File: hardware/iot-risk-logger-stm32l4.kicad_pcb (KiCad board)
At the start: 2 copper layers, 55 x 45 mm, 52 parts, among them J1 USB Type-C, J2 TagConnect SWD ARM, Q1 IRLML6401, U1 ST25DV04K, U2 OPT3001DNPR, U3 SHT30-DIS, U4 LIS2DW12, U5 AP2112K-3.3, U6 W25Q64JV, U7 STM32L412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

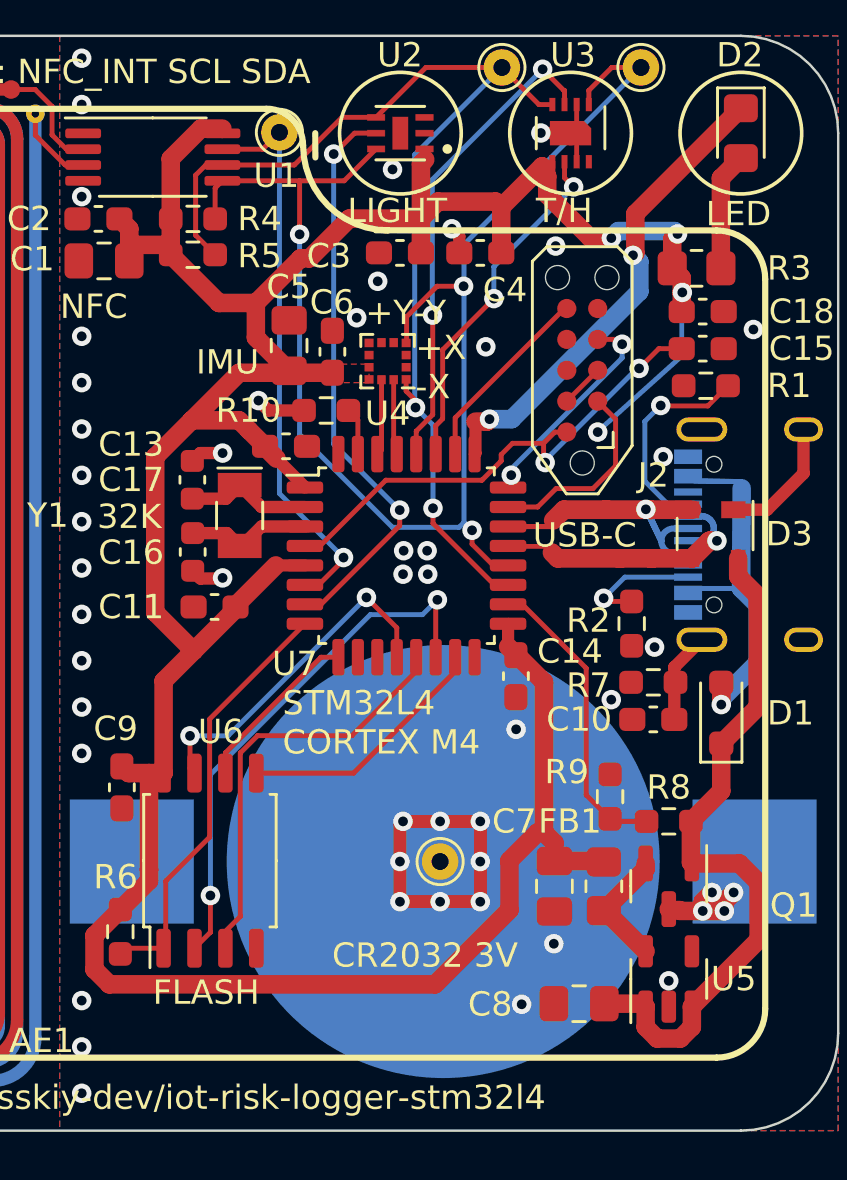
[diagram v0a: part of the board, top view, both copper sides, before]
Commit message: README: add dev tools table
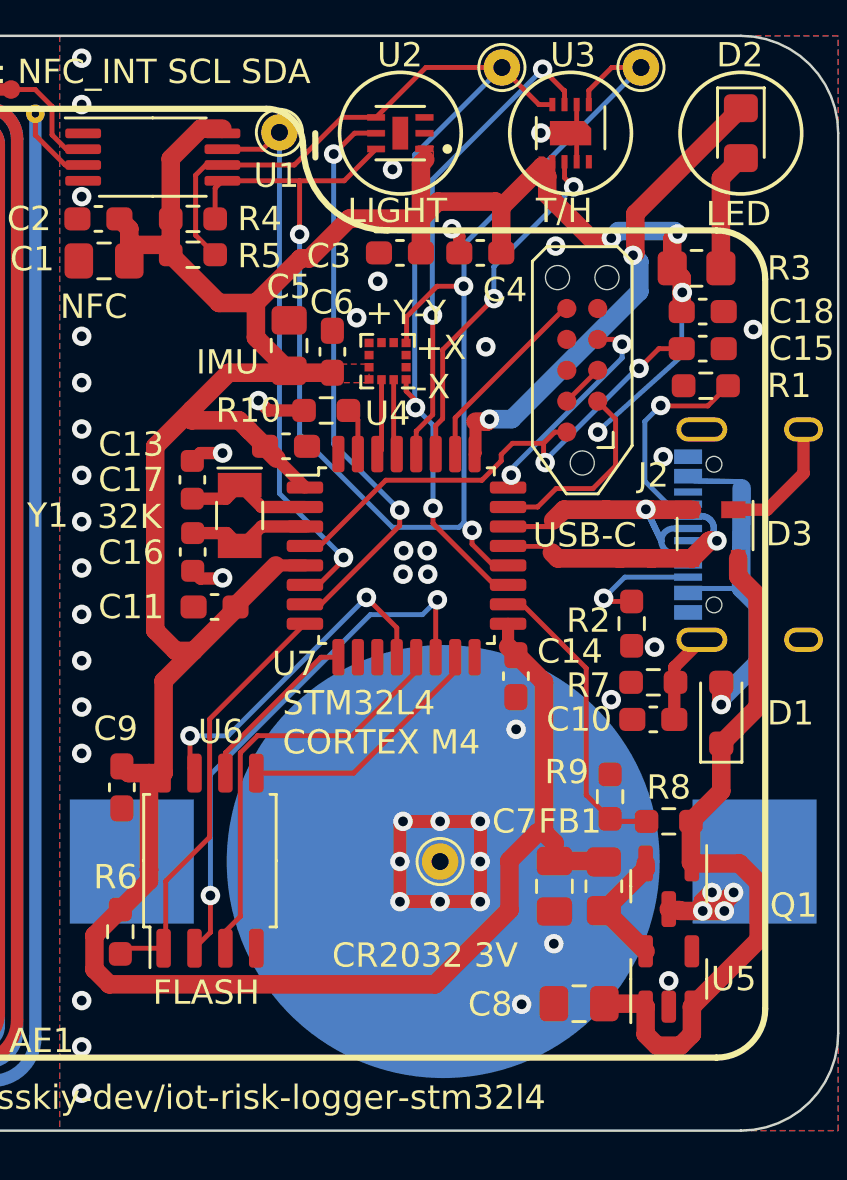
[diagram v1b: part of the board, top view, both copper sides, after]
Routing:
- net VDD: track 139.4 -> 140.5 mm
- net +5V: track 29.0 -> 29.6 mm
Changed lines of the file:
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@@
         (effects (font (size 1 1) (thickness 0.15)))
     )
-    (fp_text value "Antenna_Loop" (at -20 -20.25 unlocked) (layer "F.Fab")
+    (fp_text value "Antenna_Loop" (at -20 -20.25 unlocked) (layer "F.Fab") hide
         (effects (font (size 1 1) (thickness 0.15)))
     )
-    (fp_text user "20mil line + 10 mil spacing" (at -11.25 -25 unlocked) (layer "Dwgs.User")
+    (fp_text user "20mil line + 10 mil spacing" (at -11.25 -25 unlocked) (layer "Dwgs.User") hide
         (effects (font (size 1 1) (thickness 0.15)) (justify left bottom))
     )
-    (fp_text user "1 layer ~ 1.4uH, double layer 1.4*~3.5=~4.9uH" (at -18.25 -27 unlocked) (layer "Dwgs.User")
+    (fp_text user "1 layer ~ 1.4uH, double layer 1.4*~3.5=~4.9uH" (at -18.25 -27 unlocked) (layer "Dwgs.User") hide
         (effects (font (size 1 1) (thickness 0.15)) (justify left bottom))
     )
-    (fp_text user "${REFERENCE}" (at -24 -18.25 unlocked) (layer "F.Fab")
+    (fp_text user "${REFERENCE}" (at -24 -18.25 unlocked) (layer "F.Fab") hide
         (effects (font (size 1 1) (thickness 0.15)))
     )
@@
   (segment (start 130.8608 66.0913) (end 132.5645 66.0913) (width 0.762) (layer "F.Cu") (net 10))
   (segment (start 130.8305 87.804) (end 130.556 87.5295) (width 0.762) (layer "F.Cu") (net 10))
+  (segment (start 131.9276 74.3712) (end 133.423942 72.874858) (width 0.762) (layer "F.Cu") (net 10))
   (segment (start 146.7518 82.9323) (end 146.431 82.6115) (width 0.762) (layer "F.Cu") (net 10))
   (segment (start 132.5645 62.5494) (end 132.5645 65.024) (width 0.762) (layer "F.Cu") (net 10))
@@
   (segment (start 146.4872 91.4015) (end 146.4872 93.4308) (width 0.762) (layer "F.Cu") (net 10))
   (segment (start 138.081 76.0447) (end 138.081 76.067) (width 0.5008) (layer "F.Cu") (net 10))
+  (segment (start 133.423942 73.3044) (end 133.423942 72.874858) (width 0.762) (layer "F.Cu") (net 10))
   (segment (start 130.8608 65.4315) (end 130.8608 66.0913) (width 0.762) (layer "F.Cu") (net 10))
   (segment (start 142.8485 66.276) (end 142.8485 66.421) (width 0.762) (layer "F.Cu") (net 10))
@@
   (segment (start 142.848 66.2755) (end 142.8485 66.276) (width 0.762) (layer "F.Cu") (net 10))
   (segment (start 146.1505 65.717) (end 146.1505 66.421) (width 0.762) (layer "F.Cu") (net 10))
-  (segment (start 133.423942 73.3044) (end 135.380842 71.3475) (width 0.762) (layer "F.Cu") (net 10))
   (segment (start 132.271 84.0187) (end 133.5074 82.7823) (width 0.762) (layer "F.Cu") (net 10))
   (segment (start 134.6885 61.3125) (end 133.8014 61.3125) (width 0.762) (layer "F.Cu") (net 10))
@@
   (segment (start 142.995 62.6176) (end 142.995 62.15) (width 0.2698) (layer "F.Cu") (net 10))
   (segment (start 131.6716 91.7681) (end 131.6701 91.7696) (width 0.762) (layer "F.Cu") (net 10))
-  (segment (start 135.380842 71.3475) (end 137.43 71.3475) (width 0.762) (layer "F.Cu") (net 10))
   (segment (start 145.9208 64.3128) (end 143.5473 64.3128) (width 0.762) (layer "F.Cu") (net 10))
   (segment (start 136.9177 74.8814) (end 138.081 76.0447) (width 0.5008) (layer "F.Cu") (net 10))
@@
   (segment (start 135.2285 80.9218) (end 136.8833 79.267) (width 0.762) (layer "F.Cu") (net 10))
   (segment (start 150.3305 91.4185) (end 150.368 91.456) (width 0.762) (layer "F.Cu") (net 10))
+  (segment (start 131.9276 81.9404) (end 131.9276 74.3712) (width 0.762) (layer "F.Cu") (net 10))
   (segment (start 137.8989 66.646) (end 138.27 66.646) (width 0.762) (layer "F.Cu") (net 10))
   (segment (start 146.4872 93.4308) (end 143.4312 96.4868) (width 0.762) (layer "F.Cu") (net 10))
   (segment (start 135.2285 80.9752) (end 135.2285 80.9218) (width 0.762) (layer "F.Cu") (net 10))
   (segment (start 153.178 65.8619) (end 153.178 67.056) (width 0.762) (layer "F.Cu") (net 10))
+  (segment (start 132.7695 82.7823) (end 131.9276 81.9404) (width 0.762) (layer "F.Cu") (net 10))
   (segment (start 153.5695 68.0223) (end 153.5695 67.4475) (width 0.762) (layer "F.Cu") (net 10))
   (segment (start 136.8833 79.267) (end 138.081 79.267) (width 0.5008) (layer "F.Cu") (net 10))
@@
   (segment (start 148.336 91.4185) (end 150.3305 91.4185) (width 0.762) (layer "F.Cu") (net 10))
   (segment (start 138.27 66.646) (end 139.9039 65.0121) (width 0.762) (layer "F.Cu") (net 10))
-  (segment (start 131.9276 74.800742) (end 133.423942 73.3044) (width 0.762) (layer "F.Cu") (net 10))
   (segment (start 130.0402 96.4868) (end 129.4288 95.8754) (width 0.762) (layer "F.Cu") (net 10))
   (segment (start 130.8608 66.0913) (end 130.8608 66.7512) (width 0.762) (layer "F.Cu") (net 10))
@@
   (segment (start 147.6498 90.2389) (end 146.4872 91.4015) (width 0.762) (layer "F.Cu") (net 10))
   (segment (start 153.5695 67.4475) (end 153.178 67.056) (width 0.762) (layer "F.Cu") (net 10))
+  (segment (start 133.423942 72.874858) (end 134.9513 71.3475) (width 0.762) (layer "F.Cu") (net 10))
   (segment (start 131.6716 87.804) (end 131.6716 91.7681) (width 0.762) (layer "F.Cu") (net 10))
   (segment (start 148.25 62.675) (end 148.25 63.28) (width 0.2498) (layer "F.Cu") (net 10))
   (segment (start 136.9177 74.8814) (end 136.4405 74.4042) (width 0.762) (layer "F.Cu") (net 10))
+  (segment (start 133.5074 82.7823) (end 132.7695 82.7823) (width 0.762) (layer "F.Cu") (net 10))
   (segment (start 136.0644 69.9029) (end 137.43 71.2685) (width 0.762) (layer "F.Cu") (net 10))
   (segment (start 139.9039 65.0121) (end 142.848 65.0121) (width 0.762) (layer "F.Cu") (net 10))
   (segment (start 146.8022 82.9575) (end 146.7518 82.9575) (width 0.762) (layer "F.Cu") (net 10))
+  (segment (start 134.9513 71.3475) (end 137.43 71.3475) (width 0.762) (layer "F.Cu") (net 10))
   (segment (start 129.4288 94.4767) (end 130.493 93.4125) (width 0.762) (layer "F.Cu") (net 10))
   (segment (start 129.4288 95.8754) (end 129.4288 94.4767) (width 0.762) (layer "F.Cu") (net 10))
@@
   (segment (start 153.3959 65.644) (end 153.178 65.8619) (width 0.762) (layer "F.Cu") (net 10))
   (segment (start 143.4312 96.4868) (end 130.0402 96.4868) (width 0.762) (layer "F.Cu") (net 10))
-  (segment (start 133.5074 82.7823) (end 131.9276 81.2025) (width 0.762) (layer "F.Cu") (net 10))
   (segment (start 135.3737 73.3044) (end 135.7829 73.7136) (width 0.762) (layer "F.Cu") (net 10))
   (segment (start 153.5695 68.0709) (end 153.5938 68.0466) (width 0.762) (layer "F.Cu") (net 10))
-  (segment (start 131.9276 81.2025) (end 131.9276 74.800742) (width 0.762) (layer "F.Cu") (net 10))
   (segment (start 149.8182 65.8123) (end 148.0404 64.0345) (width 0.762) (layer "F.Cu") (net 10))
   (segment (start 136.0644 68.4805) (end 136.0644 69.9029) (width 0.762) (layer "F.Cu") (net 10))
@@
   (segment (start 155.89 78.978) (end 155.89 79.7154) (width 0.762) (layer "F.Cu") (net 31))
   (segment (start 155.9411 91.5185) (end 153.985 91.5185) (width 0.762) (layer "F.Cu") (net 31))
-  (segment (start 153.985 98.2431) (end 153.985 97.4035) (width 0.762) (layer "F.Cu") (net 31))
+  (segment (start 153.985 98.5418) (end 153.985 97.4035) (width 0.762) (layer "F.Cu") (net 31))
   (segment (start 153.985 91.5185) (end 153.9475 91.481) (width 0.762) (layer "F.Cu") (net 31))
-  (segment (start 152.085 97.4035) (end 152.085 98.2422) (width 0.762) (layer "F.Cu") (net 31))
-  (segment (start 152.5581 98.7153) (end 153.5128 98.7153) (width 0.762) (layer "F.Cu") (net 31))
   (segment (start 151.9635 97.282) (end 152.085 97.4035) (width 0.762) (layer "F.Cu") (net 31))
   (segment (start 153.9475 91.481) (end 153.9475 89.789) (width 0.762) (layer "F.Cu") (net 31))
+  (segment (start 152.085 98.5418) (end 152.5524 99.0092) (width 0.762) (layer "F.Cu") (net 31))
+  (segment (start 152.5524 99.0092) (end 153.5176 99.0092) (width 0.762) (layer "F.Cu") (net 31))
+  (segment (start 152.085 97.4035) (end 152.085 98.5418) (width 0.762) (layer "F.Cu") (net 31))
   (segment (start 155.194 86.594) (end 155.194 88.5425) (width 0.762) (layer "F.Cu") (net 31))
   (segment (start 155.89 79.7154) (end 156.6926 80.518) (width 0.762) (layer "F.Cu") (net 31))
   (segment (start 156.6926 80.518) (end 156.6926 85.0954) (width 0.762) (layer "F.Cu") (net 31))
-  (segment (start 153.5128 98.7153) (end 153.985 98.2431) (width 0.762) (layer "F.Cu") (net 31))
   (segment (start 150.3895 97.282) (end 151.9635 97.282) (width 0.762) (layer "F.Cu") (net 31))
   (segment (start 156.7306 92.308) (end 155.9411 91.5185) (width 0.762) (layer "F.Cu") (net 31))
@@
   (segment (start 153.985 97.4035) (end 156.7306 94.6579) (width 0.762) (layer "F.Cu") (net 31))
   (segment (start 155.194 88.5425) (end 153.9475 89.789) (width 0.762) (layer "F.Cu") (net 31))
-  (segment (start 152.085 98.2422) (end 152.5581 98.7153) (width 0.762) (layer "F.Cu") (net 31))
+  (segment (start 153.5176 99.0092) (end 153.985 98.5418) (width 0.762) (layer "F.Cu") (net 31))
   (segment (start 140.256 74.692) (end 140.256 73.2875) (width 0.2032) (layer "F.Cu") (net 32))
   (segment (start 140.256 73.2875) (end 139.8665 72.898) (width 0.2032) (layer "F.Cu") (net 32))
@@
     )
   )
+  (zone (net 10) (net_name "VDD") (layer "F.Cu") (hatch edge 0.5)
+    (priority 2)
+    (connect_pads yes (clearance 0))
+    (min_thickness 0.25) (filled_areas_thickness no)
+    (fill yes (thermal_gap 0) (thermal_bridge_width 0.5))
+    (polygon
+      (pts
+        (xy 142.6464 62.0268)
+        (xy 142.6464 62.484)
+        (xy 143.3576 62.484)
+        (xy 143.3576 62.0268)
+      )
+    )
+  )
   (zone (net 10) (net_name "VDD") (layer "F.Cu") (name "$teardrop_padvia$") (hatch edge 0.5)
     (priority 30002)
@@
       )
     )
+  )
+  (zone (net 10) (net_name "VDD") (layer "F.Cu") (hatch edge 0.5)
+    (priority 3)
+    (connect_pads yes (clearance 0))
+    (min_thickness 0.25) (filled_areas_thickness no)
+    (fill yes (thermal_gap 0) (thermal_bridge_width 0.5))
+    (polygon
+      (pts
+        (xy 147.6756 62.484)
+        (xy 148.336 62.484)
+        (xy 148.336 62.8396)
+        (xy 147.6756 62.8396)
+      )
+    )

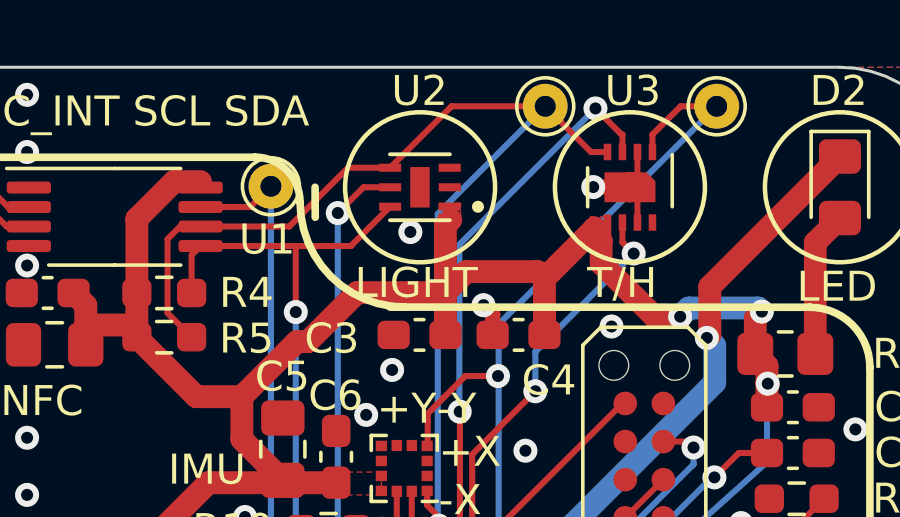
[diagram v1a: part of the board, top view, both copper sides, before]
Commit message: README: update schematics
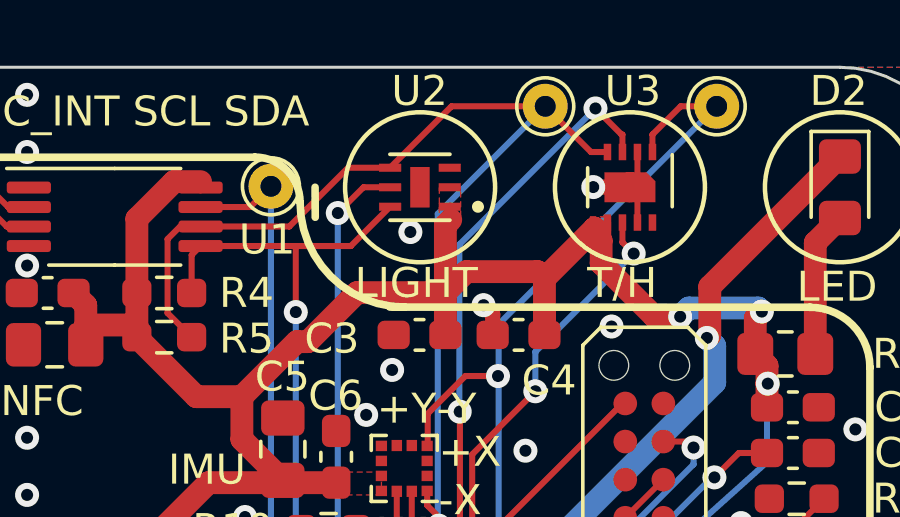
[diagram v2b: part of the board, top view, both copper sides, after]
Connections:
- J1 pad s1: /GND_SHIELD -> (no net)
- U2 pad 2: GND -> VDD
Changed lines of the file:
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@@
       (net 10 "VDD") (pinfunction "VDD") (pintype "power_in"))
     (pad "2" smd roundrect (at -0.995 0 180) (size 0.74 0.27) (layers "F.Cu" "F.Paste" "F.Mask") (roundrect_rratio 0.03)
-      (net 1 "GND") (pinfunction "ADDR") (pintype "input"))
+      (net 10 "VDD") (pinfunction "ADDR") (pintype "input"))
     (pad "3" smd roundrect (at -0.995 0.65 180) (size 0.74 0.27) (layers "F.Cu" "F.Paste" "F.Mask") (roundrect_rratio 0.03)
       (net 1 "GND") (pinfunction "GND") (pintype "power_in"))
@@
     (fp_line (start 4.47 -3.675) (end 4.47 3.675)
       (stroke (width 0.1) (type solid)) (layer "B.Fab"))
-    (pad "" thru_hole oval (at -4.32 3.105 270) (size 1 2.1) (drill oval 0.6 1.7) (layers "*.Cu" "*.Mask")
-      (pinfunction "SHIELD") (pintype "passive"))
+    (pad "" thru_hole oval (at -4.32 3.105 270) (size 1 2.1) (drill oval 0.6 1.7) (layers "*.Cu" "*.Mask"))
     (pad "" np_thru_hole circle (at -2.89 2.605 270) (size 0.65 0.65) (drill 0.65) (layers "*.Cu" "*.Mask"))
     (pad "" np_thru_hole circle (at 2.89 2.605 270) (size 0.65 0.65) (drill 0.65) (layers "*.Cu" "*.Mask"))
-    (pad "" thru_hole oval (at 4.32 -1.075 270) (size 1 1.6) (drill oval 0.6 1.2) (layers "*.Cu" "*.Mask")
-      (pinfunction "SHIELD") (pintype "passive"))
+    (pad "" thru_hole oval (at 4.32 -1.075 270) (size 1 1.6) (drill oval 0.6 1.2) (layers "*.Cu" "*.Mask"))
     (pad "A1" smd rect (at -3.35 3.67 270) (size 0.3 1.15) (layers "B.Cu" "B.Paste" "B.Mask")
       (net 1 "GND") (pinfunction "GND") (pintype "passive"))
@@
     (pad "S1" thru_hole oval (at -4.32 -1.075 270) (size 1 1.6) (drill oval 0.6 1.2) (layers "*.Cu" "*.Mask")
       (net 5 "/GND_SHIELD") (pinfunction "SHIELD") (pintype "passive"))
-    (pad "s1" thru_hole oval (at 4.32 3.105 270) (size 1 2.1) (drill oval 0.6 1.7) (layers "*.Cu" "*.Mask")
-      (net 5 "/GND_SHIELD") (pinfunction "SHIELD") (pintype "passive"))
+    (pad "s1" thru_hole oval (at 4.32 3.105 270) (size 1 2.1) (drill oval 0.6 1.7) (layers "*.Cu" "*.Mask"))
     (model "/Users/artempolisskyi/Documents/KiCad/6.0/3dmodels/CSP-USC16-TR--3DModel-STEP-468060.STEP"
       (offset (xyz 0 2.5 0))
@@
     (polygon
       (pts
-        (xy 142.6464 62.0268)
+        (xy 142.6464 61.5188)
         (xy 142.6464 62.484)
         (xy 143.3576 62.484)
-        (xy 143.3576 62.0268)
+        (xy 143.3576 61.5188)
       )
     )
